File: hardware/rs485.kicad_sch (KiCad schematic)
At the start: 0 parts

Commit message: Almost everything
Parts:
- added U13: MAX3485AEASA+T, EasyEDA:SO-8_L4.9-W3.9-P1.27-LS5.9-BL, symbol EasyEDA:MAX3485AEASA+T
- added U14: KF301-5.0-2P, EasyEDA:CONN-TH_P5.00_KF301-5.0-2P, symbol EasyEDA:KF301-5.0-2P
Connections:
- new net +3V3: U13.8 (VCC)
- new net GND: U13.5 (GND)
- new net RS485_A: U13.6 (A), U14.2
- new net RS485_B: U13.7 (B), U14.1
- new net RS485_MODE: U13.2 (~{RE}), U13.3 (DE)
- new net UART_RX: U13.1 (RO)
- new net UART_TX: U13.4 (DI)

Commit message: Board complete
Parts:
- removed U13: MAX3485AEASA+T, EasyEDA:SO-8_L4.9-W3.9-P1.27-LS5.9-BL, symbol EasyEDA:MAX3485AEASA+T
- removed U14: KF301-5.0-2P, EasyEDA:CONN-TH_P5.00_KF301-5.0-2P, symbol EasyEDA:KF301-5.0-2P
- added C17: 0.1uF, Capacitor_SMD:C_1206_3216Metric_Pad1.33x1.80mm_HandSolder, symbol Device:C
- added D8: CDSOT23-SM712, Samacsys:SOT95P230X117-3N, symbol Samacsys:CDSOT23-SM712
- added IC2: SN65HVD75DGKR, Samacsys:SOP65P490X110-8N, symbol Samacsys:SN65HVD75DGKR
- added J13: 39880-0303, Samacsys:398800303, symbol Samacsys:39880-0303
- added R33, R34: 10k, Resistor_SMD:R_1206_3216Metric_Pad1.30x1.75mm_HandSolder, symbol Device:R
- added R35: 120R, Resistor_SMD:R_1206_3216Metric_Pad1.30x1.75mm_HandSolder, symbol Device:R
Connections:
- net +3V3: now also C17.1, IC2.8 (VCC), R33.1
- net GND: now also C17.2, D8.3, IC2.5 (GND), J13.3, R34.2
- net RS485_MODE: now also IC2.2 (~{RE}), IC2.3 (DE), R34.1
- net UART_RX: now also IC2.1 (R), R33.2
- net UART_TX: now also IC2.4 (D)
- new net RS485+: D8.2, IC2.7 (B), J13.1, R35.1
- new net RS485-: D8.1, IC2.6 (A), J13.2, R35.2
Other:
- note added: "0 ohm jumpers or 10K pullups (need to test, if need - datasheet)"
- note added: "TVS diode for protection"

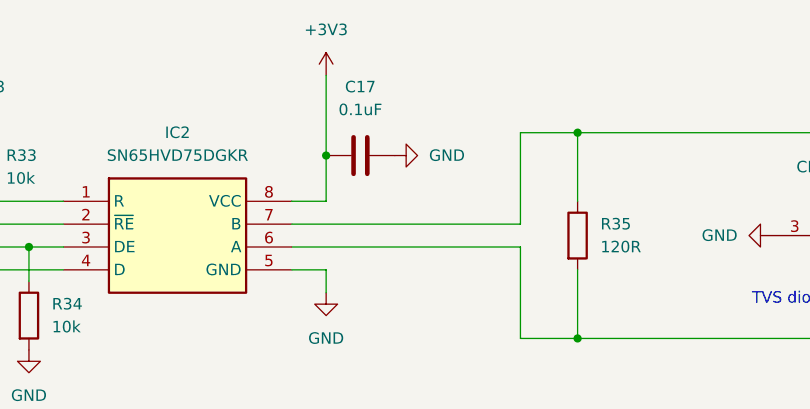
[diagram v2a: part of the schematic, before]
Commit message: Modbus, small schematic changes
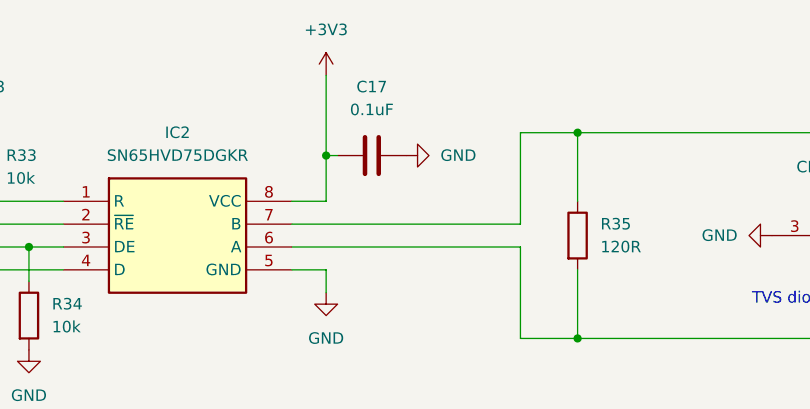
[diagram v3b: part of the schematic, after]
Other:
- moved on the sheet: C17
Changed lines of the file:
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@@
+	(wire
+		(pts
+			(xy 92.71 38.1) (xy 91.44 38.1)
+		)
+		(stroke
+			(width 0)
+			(type default)
+		)
+	)
 	(wire
 		(pts
@@
 	(symbol
 		(lib_id "Device:C")
-		(at 95.25 38.1 90)
+		(at 96.52 38.1 90)
 		(unit 1)
 		(exclude_from_sim no)
@@
 		(fields_autoplaced yes)
 		(property "Reference" "C17"
-			(at 95.25 30.48 90)
+			(at 96.52 30.48 90)
 			(effects
 				(font
@@
 		)
 		(property "Value" "0.1uF"
-			(at 95.25 33.02 90)
+			(at 96.52 33.02 90)
 			(effects
 				(font
@@
 		)
 		(property "Footprint" "Capacitor_SMD:C_1206_3216Metric_Pad1.33x1.80mm_HandSolder"
-			(at 99.06 37.1348 0)
+			(at 100.33 37.1348 0)
 			(effects
 				(font
@@
 		)
 		(property "Datasheet" "~"
-			(at 95.25 38.1 0)
+			(at 96.52 38.1 0)
 			(effects
 				(font
@@
 		)
 		(property "Description" "Unpolarized capacitor"
-			(at 95.25 38.1 0)
+			(at 96.52 38.1 0)
 			(effects
 				(font
@@
 	(symbol
 		(lib_id "power:GND")
-		(at 99.06 38.1 90)
+		(at 100.33 38.1 90)
 		(unit 1)
 		(exclude_from_sim no)
@@
 		(fields_autoplaced yes)
 		(property "Reference" "#PWR065"
-			(at 105.41 38.1 0)
+			(at 106.68 38.1 0)
 			(effects
 				(font
@@
 		)
 		(property "Value" "GND"
-			(at 102.87 38.0999 90)
+			(at 104.14 38.0999 90)
 			(effects
 				(font
@@
 		)
 		(property "Footprint" ""
-			(at 99.06 38.1 0)
+			(at 100.33 38.1 0)
 			(effects
 				(font
@@
 		)
 		(property "Datasheet" ""
-			(at 99.06 38.1 0)
+			(at 100.33 38.1 0)
 			(effects
 				(font
@@
 		)
 		(property "Description" "Power symbol creates a global label with name \"GND\" , ground"
-			(at 99.06 38.1 0)
-			(effects
-				(font
+			(at 100.33 38.1 0)
+			(effects
+				(font

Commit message: UART parity and better timing handling
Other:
- title: (none) -> RS-485
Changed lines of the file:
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@@
 	(generator_version "9.0")
 	(paper "A4")
+	(title_block
+		(title "RS-485")
+	)
 	(text "0 ohm jumpers or 10K pullups\n(need to test, if need - datasheet)"
 		(exclude_from_sim no)
